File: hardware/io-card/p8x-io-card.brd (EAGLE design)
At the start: 160 x 100 mm, 56 parts, among them J1 DIN41612-96M, J2 SERIAL, J3 RTC 3-WIRE, SW1 INPUT, U1 IO PAGE, U10 LED PORT, U11 MON A-LO, U12 MON A-HI, U13 MON D, U14 ACIA, U15 74HCT00, U16 RTC DNP, U2 PORT DEC, U3 DOE DEC, U4 DLD DEC, U5 74HCT32, U6 74HCT08, U7 BAUD DIV, U8 RS232, U9 SW IN, X2 2.4576MHZ, X3 32.768KHZ

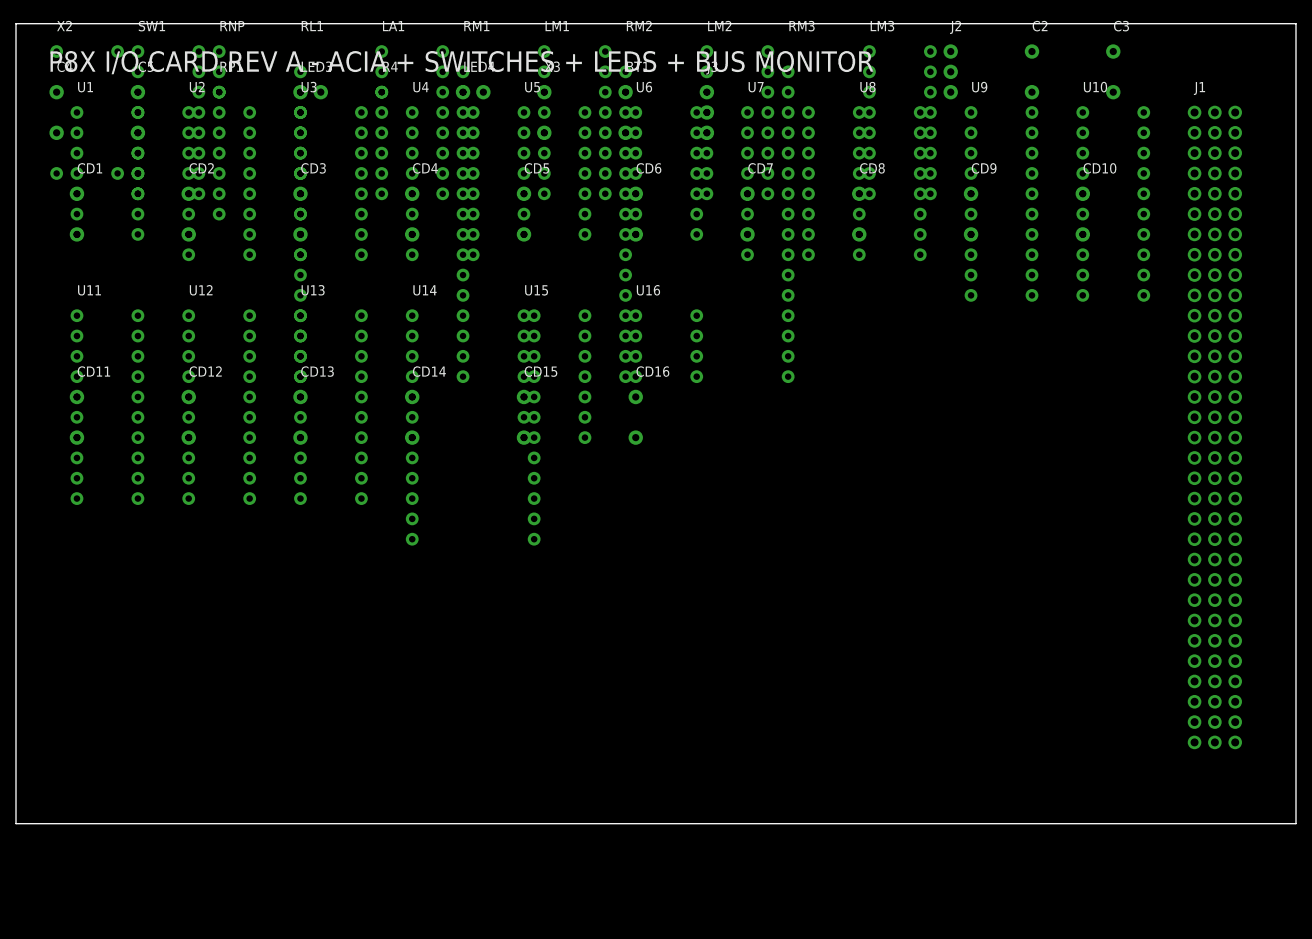
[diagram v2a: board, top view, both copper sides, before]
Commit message: feat(hw): footprint-aware placement (no component overlaps) + overlap guard
The old auto-placer used a fixed 13.97x25.4mm grid that was tighter than real
footprints — tall DIPs collided with the row below and per-IC caps were buried.

- card(): place by each part's real pad-extent + clearance, flowing in rows that
  wrap at the board width and stack downward (J1 hugs the left edge). Guarantees
  no overlaps. Dense cards (ALU, regbank) now run past the 160x100 outline — they
  genuinely don't fit at safe pitch; arrange by hand when routing (the placement
  PDF flags the overflow).
- memory card: relocate the 9 decoupling caps to a clear bottom strip (they sat
  under the tall DIP-28W ICs).
- validate(): add a rotation-aware footprint-overlap guard (board files) so a
  future card can't silently reintroduce overlaps.
- Regenerated all boards + placement/schematic PDFs.

Verified: 0 overlaps across all 7 boards (rotation-aware); 0 validation errors;
all 6 test suites pass.

Co-Authored-By: Claude Opus 4.8 <noreply@anthropic.com>
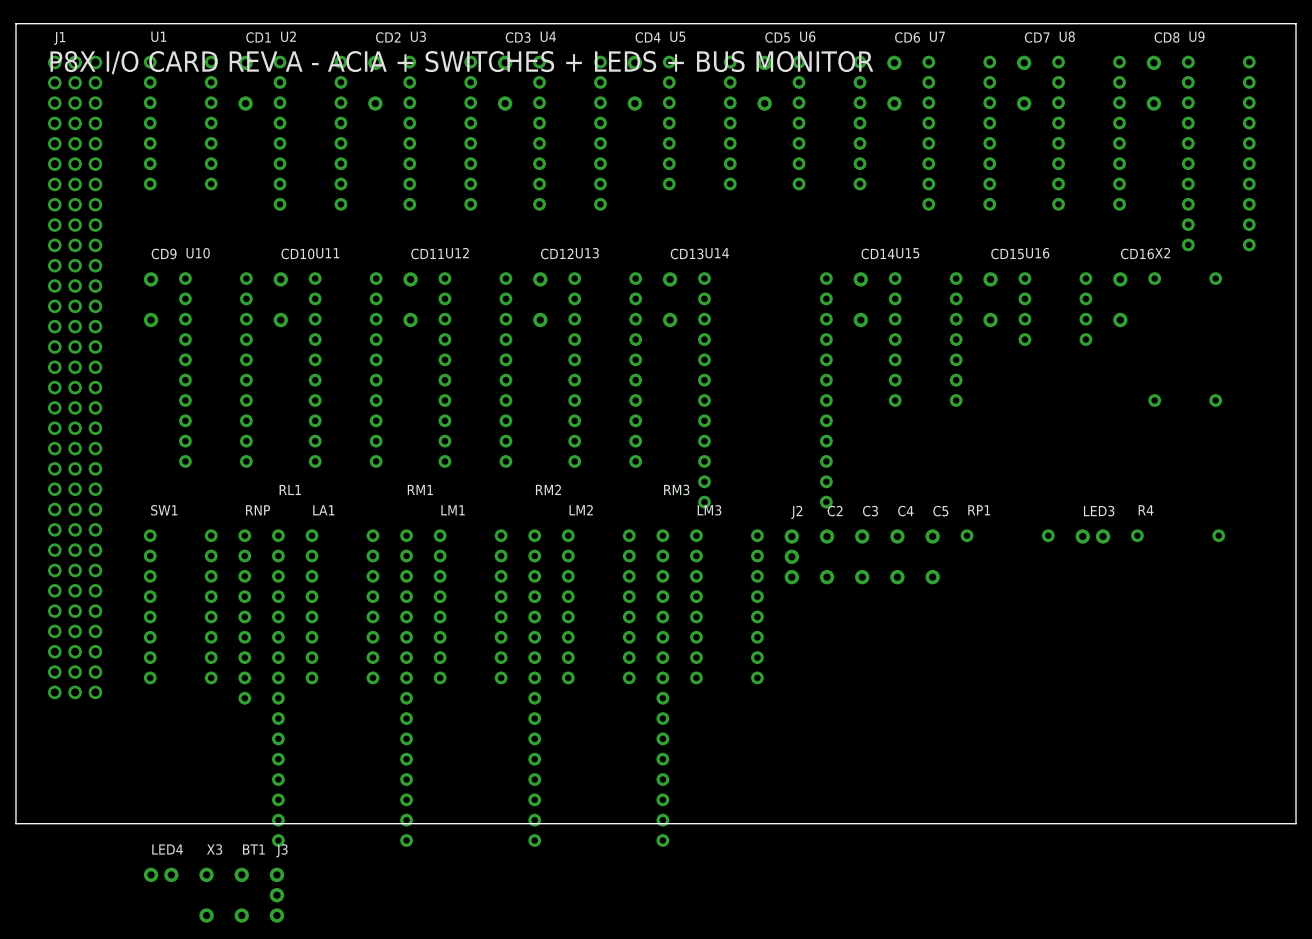
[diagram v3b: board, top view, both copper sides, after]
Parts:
- moved J1 142.6 mm to (4.85, 95.2)
- moved X2 140.2 mm to (142.3, 68.1)
- moved C4 118.9 mm to (110.2, 35.9)
- moved U10 114.1 mm to (21.2, 68.1)
- moved C5 113.8 mm to (114.6, 35.9)
- moved LED3 112.5 mm to (133.3, 35.9)
- moved J3 111.6 mm to (32.6, -6.40)
- moved R4 109.5 mm to (140.2, 36.0)
- moved BT1 109.0 mm to (28.2, -6.40)
- moved RP1 108.7 mm to (118.9, 36.0)
- moved X3 106.6 mm to (23.8, -6.40)
- moved LED4 105.3 mm to (16.9, -6.40)
- moved CD9 103.1 mm to (16.9, 68.0)
- moved CD10 100.8 mm to (33.1, 68.0)
- moved C3 68.3 mm to (105.8, 35.9)
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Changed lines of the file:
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@@
 <designrules name="default"><param name="layerSetup" value="(1*2*15*16)"/></designrules>
 <elements>
-<element name="J1" library="p8x" package="DIN96" value="DIN41612-96M" x="147.32" y="88.90"/>
-<element name="U1" library="p8x" package="DIP14" value="IO PAGE" x="7.62" y="88.90"/>
-<element name="CD1" library="p8x" package="C_DISC" value="100N" x="7.62" y="78.74"/>
-<element name="U2" library="p8x" package="DIP16" value="PORT DEC" x="21.59" y="88.90"/>
-<element name="CD2" library="p8x" package="C_DISC" value="100N" x="21.59" y="78.74"/>
-<element name="U3" library="p8x" package="DIP16" value="DOE DEC" x="35.56" y="88.90"/>
-<element name="CD3" library="p8x" package="C_DISC" value="100N" x="35.56" y="78.74"/>
-<element name="U4" library="p8x" package="DIP16" value="DLD DEC" x="49.53" y="88.90"/>
-<element name="CD4" library="p8x" package="C_DISC" value="100N" x="49.53" y="78.74"/>
-<element name="U5" library="p8x" package="DIP14" value="74HCT32" x="63.50" y="88.90"/>
-<element name="CD5" library="p8x" package="C_DISC" value="100N" x="63.50" y="78.74"/>
-<element name="U6" library="p8x" package="DIP14" value="74HCT08" x="77.47" y="88.90"/>
-<element name="CD6" library="p8x" package="C_DISC" value="100N" x="77.47" y="78.74"/>
-<element name="U7" library="p8x" package="DIP16" value="BAUD DIV" x="91.44" y="88.90"/>
-<element name="CD7" library="p8x" package="C_DISC" value="100N" x="91.44" y="78.74"/>
-<element name="U8" library="p8x" package="DIP16" value="RS232" x="105.41" y="88.90"/>
-<element name="CD8" library="p8x" package="C_DISC" value="100N" x="105.41" y="78.74"/>
-<element name="U9" library="p8x" package="DIP20" value="SW IN" x="119.38" y="88.90"/>
-<element name="CD9" library="p8x" package="C_DISC" value="100N" x="119.38" y="78.74"/>
-<element name="U10" library="p8x" package="DIP20" value="LED PORT" x="133.35" y="88.90"/>
-<element name="CD10" library="p8x" package="C_DISC" value="100N" x="133.35" y="78.74"/>
-<element name="U11" library="p8x" package="DIP20" value="MON A-LO" x="7.62" y="63.50"/>
-<element name="CD11" library="p8x" package="C_DISC" value="100N" x="7.62" y="53.34"/>
-<element name="U12" library="p8x" package="DIP20" value="MON A-HI" x="21.59" y="63.50"/>
-<element name="CD12" library="p8x" package="C_DISC" value="100N" x="21.59" y="53.34"/>
-<element name="U13" library="p8x" package="DIP20" value="MON D" x="35.56" y="63.50"/>
-<element name="CD13" library="p8x" package="C_DISC" value="100N" x="35.56" y="53.34"/>
-<element name="U14" library="p8x" package="DIP24W" value="ACIA" x="49.53" y="63.50"/>
-<element name="CD14" library="p8x" package="C_DISC" value="100N" x="49.53" y="53.34"/>
-<element name="U15" library="p8x" package="DIP14" value="74HCT00" x="63.50" y="63.50"/>
-<element name="CD15" library="p8x" package="C_DISC" value="100N" x="63.50" y="53.34"/>
-<element name="U16" library="p8x" package="DIP8" value="RTC DNP" x="77.47" y="63.50"/>
-<element name="CD16" library="p8x" package="C_DISC" value="100N" x="77.47" y="53.34"/>
-<element name="X2" library="p8x" package="OSC4" value="2.4576MHZ" x="5.08" y="96.52"/>
-<element name="SW1" library="p8x" package="DIP16" value="INPUT" x="15.24" y="96.52"/>
-<element name="RNP" library="p8x" package="SIP9" value="8X10K" x="25.40" y="96.52"/>
-<element name="RL1" library="p8x" package="SIP16" value="8X330R" x="35.56" y="96.52"/>
-<element name="LA1" library="p8x" package="DIP16" value="PORT LEDS" x="45.72" y="96.52"/>
-<element name="RM1" library="p8x" package="SIP16" value="8X330R" x="55.88" y="96.52"/>
-<element name="LM1" library="p8x" package="DIP16" value="A0-7" x="66.04" y="96.52"/>
-<element name="RM2" library="p8x" package="SIP16" value="8X330R" x="76.20" y="96.52"/>
-<element name="LM2" library="p8x" package="DIP16" value="A8-15" x="86.36" y="96.52"/>
-<element name="RM3" library="p8x" package="SIP16" value="8X330R" x="96.52" y="96.52"/>
-<element name="LM3" library="p8x" package="DIP16" value="D0-7" x="106.68" y="96.52"/>
-<element name="J2" library="p8x" package="HDR3" value="SERIAL" x="116.84" y="96.52"/>
-<element name="C2" library="p8x" package="C_DISC" value="1U" x="127.00" y="96.52"/>
-<element name="C3" library="p8x" package="C_DISC" value="1U" x="137.16" y="96.52"/>
-<element name="C4" library="p8x" package="C_DISC" value="1U" x="5.08" y="91.44"/>
-<element name="C5" library="p8x" package="C_DISC" value="1U" x="15.24" y="91.44"/>
-<element name="RP1" library="p8x" package="R_AXIAL" value="1K" x="25.40" y="91.44"/>
-<element name="LED3" library="p8x" package="LED5" value="PWR-GRN" x="35.56" y="91.44"/>
-<element name="R4" library="p8x" package="R_AXIAL" value="1K" x="45.72" y="91.44"/>
-<element name="LED4" library="p8x" package="LED5" value="IOSEL-YEL" x="55.88" y="91.44"/>
-<element name="X3" library="p8x" package="C_DISC" value="32.768KHZ" x="66.04" y="91.44"/>
-<element name="BT1" library="p8x" package="CP_RADIAL" value="CR2032" x="76.20" y="91.44"/>
-<element name="J3" library="p8x" package="HDR3" value="RTC 3-WIRE" x="86.36" y="91.44"/>
+<element name="J1" library="p8x" package="DIN96" value="DIN41612-96M" x="4.85" y="95.15"/>
+<element name="U1" library="p8x" package="DIP14" value="IO PAGE" x="16.78" y="95.20"/>
+<element name="CD1" library="p8x" package="C_DISC" value="100N" x="28.70" y="95.10"/>
+<element name="U2" library="p8x" package="DIP16" value="PORT DEC" x="33.00" y="95.20"/>
+<element name="CD2" library="p8x" package="C_DISC" value="100N" x="44.92" y="95.10"/>
+<element name="U3" library="p8x" package="DIP16" value="DOE DEC" x="49.22" y="95.20"/>
+<element name="CD3" library="p8x" package="C_DISC" value="100N" x="61.14" y="95.10"/>
+<element name="U4" library="p8x" package="DIP16" value="DLD DEC" x="65.44" y="95.20"/>
+<element name="CD4" library="p8x" package="C_DISC" value="100N" x="77.36" y="95.10"/>
+<element name="U5" library="p8x" package="DIP14" value="74HCT32" x="81.66" y="95.20"/>
+<element name="CD5" library="p8x" package="C_DISC" value="100N" x="93.58" y="95.10"/>
+<element name="U6" library="p8x" package="DIP14" value="74HCT08" x="97.88" y="95.20"/>
+<element name="CD6" library="p8x" package="C_DISC" value="100N" x="109.80" y="95.10"/>
+<element name="U7" library="p8x" package="DIP16" value="BAUD DIV" x="114.10" y="95.20"/>
+<element name="CD7" library="p8x" package="C_DISC" value="100N" x="126.02" y="95.10"/>
+<element name="U8" library="p8x" package="DIP16" value="RS232" x="130.32" y="95.20"/>
+<element name="CD8" library="p8x" package="C_DISC" value="100N" x="142.24" y="95.10"/>
+<element name="U9" library="p8x" package="DIP20" value="SW IN" x="146.54" y="95.20"/>
+<element name="CD9" library="p8x" package="C_DISC" value="100N" x="16.88" y="68.04"/>
+<element name="U10" library="p8x" package="DIP20" value="LED PORT" x="21.18" y="68.14"/>
+<element name="CD10" library="p8x" package="C_DISC" value="100N" x="33.10" y="68.04"/>
+<element name="U11" library="p8x" package="DIP20" value="MON A-LO" x="37.40" y="68.14"/>
+<element name="CD11" library="p8x" package="C_DISC" value="100N" x="49.32" y="68.04"/>
+<element name="U12" library="p8x" package="DIP20" value="MON A-HI" x="53.62" y="68.14"/>
+<element name="CD12" library="p8x" package="C_DISC" value="100N" x="65.54" y="68.04"/>
+<element name="U13" library="p8x" package="DIP20" value="MON D" x="69.84" y="68.14"/>
+<element name="CD13" library="p8x" package="C_DISC" value="100N" x="81.76" y="68.04"/>
+<element name="U14" library="p8x" package="DIP24W" value="ACIA" x="86.06" y="68.14"/>
+<element name="CD14" library="p8x" package="C_DISC" value="100N" x="105.60" y="68.04"/>
+<element name="U15" library="p8x" package="DIP14" value="74HCT00" x="109.90" y="68.14"/>
+<element name="CD15" library="p8x" package="C_DISC" value="100N" x="121.82" y="68.04"/>
+<element name="U16" library="p8x" package="DIP8" value="RTC DNP" x="126.12" y="68.14"/>
+<element name="CD16" library="p8x" package="C_DISC" value="100N" x="138.04" y="68.04"/>
+<element name="X2" library="p8x" package="OSC4" value="2.4576MHZ" x="142.34" y="68.14"/>
+<element name="SW1" library="p8x" package="DIP16" value="INPUT" x="16.78" y="36.00"/>
+<element name="RNP" library="p8x" package="SIP9" value="8X10K" x="28.60" y="36.00"/>
+<element name="RL1" library="p8x" package="SIP16" value="8X330R" x="32.80" y="38.54"/>
+<element name="LA1" library="p8x" package="DIP16" value="PORT LEDS" x="37.00" y="36.00"/>
+<element name="RM1" library="p8x" package="SIP16" value="8X330R" x="48.82" y="38.54"/>
+<element name="LM1" library="p8x" package="DIP16" value="A0-7" x="53.02" y="36.00"/>
+<element name="RM2" library="p8x" package="SIP16" value="8X330R" x="64.84" y="38.54"/>
+<element name="LM2" library="p8x" package="DIP16" value="A8-15" x="69.04" y="36.00"/>
+<element name="RM3" library="p8x" package="SIP16" value="8X330R" x="80.86" y="38.54"/>
+<element name="LM3" library="p8x" package="DIP16" value="D0-7" x="85.06" y="36.00"/>
+<element name="J2" library="p8x" package="HDR3" value="SERIAL" x="96.98" y="35.90"/>
+<element name="C2" library="p8x" package="C_DISC" value="1U" x="101.38" y="35.90"/>
+<element name="C3" library="p8x" package="C_DISC" value="1U" x="105.78" y="35.90"/>
+<element name="C4" library="p8x" package="C_DISC" value="1U" x="110.18" y="35.90"/>
+<element name="C5" library="p8x" package="C_DISC" value="1U" x="114.58" y="35.90"/>
+<element name="RP1" library="p8x" package="R_AXIAL" value="1K" x="118.88" y="36.00"/>
+<element name="LED3" library="p8x" package="LED5" value="PWR-GRN" x="133.34" y="35.90"/>
+<element name="R4" library="p8x" package="R_AXIAL" value="1K" x="140.18" y="36.00"/>
+<element name="LED4" library="p8x" package="LED5" value="IOSEL-YEL" x="16.88" y="-6.40"/>
+<element name="X3" library="p8x" package="C_DISC" value="32.768KHZ" x="23.82" y="-6.40"/>
+<element name="BT1" library="p8x" package="CP_RADIAL" value="CR2032" x="28.22" y="-6.40"/>
+<element name="J3" library="p8x" package="HDR3" value="RTC 3-WIRE" x="32.62" y="-6.40"/>
 </elements><signals>
 <signal name="-MEMW">

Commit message: fix(bom): card DIN connectors were undercounted (1 -> 6); label them FABC96R
Two fixes:
- card() built CARDS[name] from `allp`, which omitted J1 — so the 5 plug-in
  cards' DIN41612 edge connectors never reached the BOM (it showed qty 1, only
  the memory card's J1). Include J1 in allp (the schematic renderer already
  filters J1 by name, so rendering is unchanged). BOM now correctly shows 6 card
  connectors + 10 backplane receptacles.
- Card edge connector is FABC96R (user-specified): set the value label on every
  card J1 and name it in the BOM; backplane receptacles noted as the mating part.

Regenerated all boards + PDFs + BOM; all 6 test suites pass.

Co-Authored-By: Claude Opus 4.8 <noreply@anthropic.com>
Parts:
- J1: value DIN41612-96M -> FABC96R
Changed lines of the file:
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@@
 <designrules name="default"><param name="layerSetup" value="(1*2*15*16)"/></designrules>
 <elements>
-<element name="J1" library="p8x" package="DIN96" value="DIN41612-96M" x="4.85" y="95.15"/>
+<element name="J1" library="p8x" package="DIN96" value="FABC96R" x="4.85" y="95.15"/>
 <element name="U1" library="p8x" package="DIP14" value="IO PAGE" x="16.78" y="95.20"/>
 <element name="CD1" library="p8x" package="C_DISC" value="100N" x="28.70" y="95.10"/>
